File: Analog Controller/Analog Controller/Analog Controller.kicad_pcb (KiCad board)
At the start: 4 copper layers, 76.2 x 71.1 mm, 63 parts, among them J1 MINIFIT-2-VERT, J2 Conn_02x08_Counter_Clockwise, J3 Conn_02x08_Counter_Clockwise, J4 MINIFIT-2-VERT, J5 Conn_01x04, J6 MINIFIT-2-VERT, J7 Conn_02x09_Counter_Clockwise, J8 Conn_02x08_Counter_Clockwise, J9 284697-E, SW2 SW_Omron_B3FS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

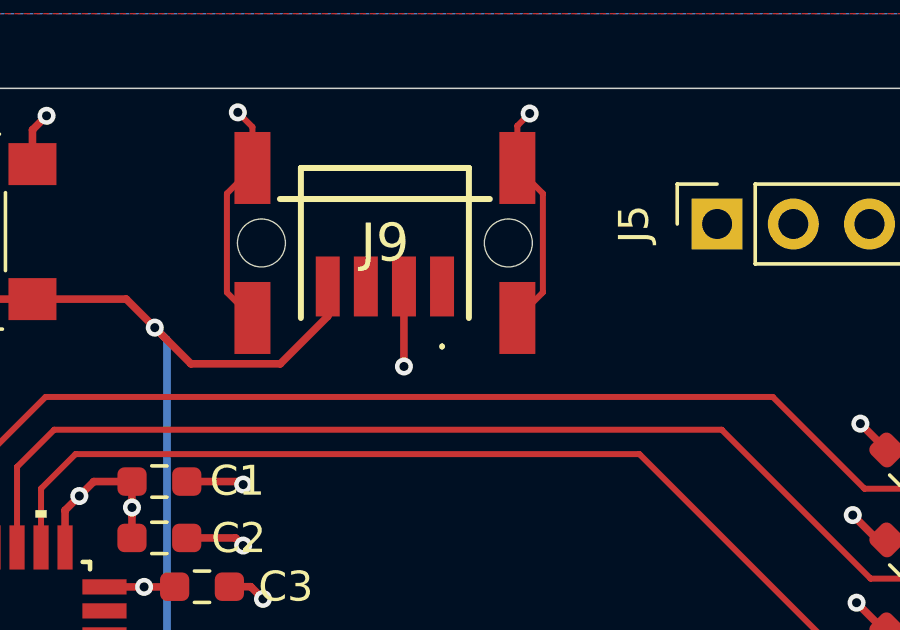
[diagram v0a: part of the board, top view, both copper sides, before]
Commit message: Reduced minimum clearance on digicorder
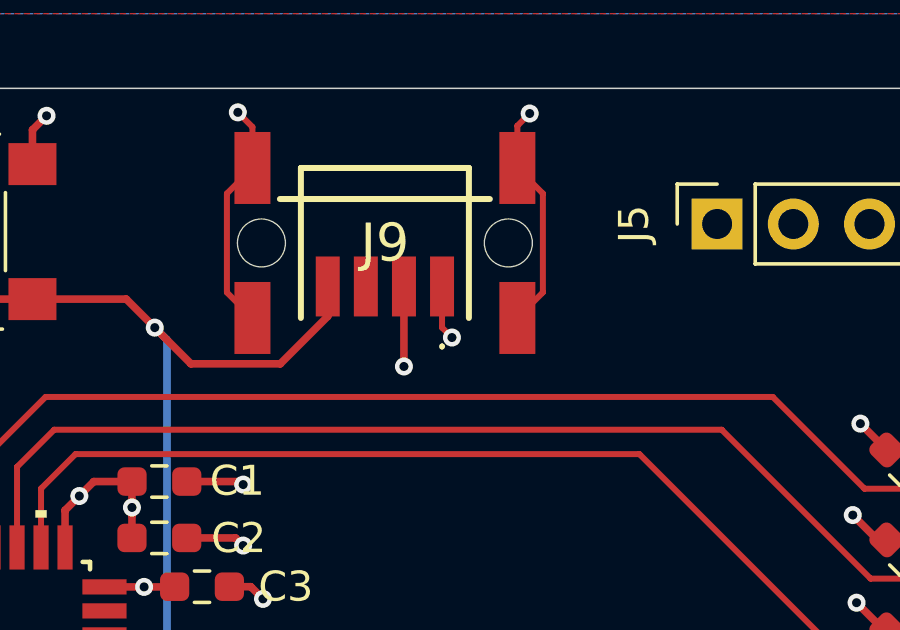
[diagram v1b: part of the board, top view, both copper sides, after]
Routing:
- net +3V3: track 28.5 -> 30.3 mm, vias 14 -> 15
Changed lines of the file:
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@@
+	)
+	(segment
+		(start 72.1614 33.3756)
+		(end 72.4916 33.7058)
+		(width 0.2)
+		(layer "F.Cu")
+		(net 2)
 	)
 	(segment
@@
 		(net 2)
 	)
+	(segment
+		(start 72.1614 32.004)
+		(end 72.1614 33.3756)
+		(width 0.2)
+		(layer "F.Cu")
+		(net 2)
+	)
 	(via
 		(at 63.3495 53.086)
@@
 		(size 0.6)
 		(drill 0.3)
+		(layers "F.Cu" "B.Cu")
+		(net 2)
+	)
+	(via
+		(at 72.4916 33.7058)
+		(size 0.6)
+		(drill 0.3)

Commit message: Added new stm32 microcontroller, redid pcb layout
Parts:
- removed C1, C20: 100n, Resistor_SMD:R_0603_1608Metric_Pad0.98x0.95mm_HandSolder
- removed C19, C3: 1u, Resistor_SMD:R_0603_1608Metric_Pad0.98x0.95mm_HandSolder
- removed C2: 10n, Resistor_SMD:R_0603_1608Metric_Pad0.98x0.95mm_HandSolder
- removed G***: LOGO, LOGO
- removed J5: Conn_01x04, Connector_PinSocket_2.54mm:PinSocket_1x04_P2.54mm_Vertical
- removed J9: 284697-E, 284697-E:284697E
- removed R10, R9: 4.7k, Resistor_SMD:R_0603_1608Metric_Pad0.98x0.95mm_HandSolder
- removed U10: TCA9535DBR, Package_SO:SSOP-24_5.3x8.2mm_P0.65mm
- removed U9: STM8L152K4T6, STM8L152K4T6:LQFP-32
- added C21: 10u, Resistor_SMD:R_0603_1608Metric_Pad0.98x0.95mm_HandSolder, F.Cu at (70.7, 45.6)
- added C22: 0.1u, Resistor_SMD:R_0603_1608Metric_Pad0.98x0.95mm_HandSolder, F.Cu at (54.5, 54.6)
- added C23: 0.1u, Resistor_SMD:R_0603_1608Metric_Pad0.98x0.95mm_HandSolder, F.Cu at (52.9, 42.8)
- added C24: 0.1u, Resistor_SMD:R_0603_1608Metric_Pad0.98x0.95mm_HandSolder, F.Cu at (54.9, 40.5)
- added C25: 0.1u, Resistor_SMD:R_0603_1608Metric_Pad0.98x0.95mm_HandSolder, F.Cu at (70.7, 43.8)
- added C26: 10n, Resistor_SMD:R_0603_1608Metric_Pad0.98x0.95mm_HandSolder, B.Cu at (63.4, 57.6)
- added C27: 1u, Resistor_SMD:R_0603_1608Metric_Pad0.98x0.95mm_HandSolder, B.Cu at (65.0, 57.6)
- added C28: 0.1u, Resistor_SMD:R_0603_1608Metric_Pad0.98x0.95mm_HandSolder, F.Cu at (51.6, 35.4)
- added C29: 0.1u, Resistor_SMD:R_0603_1608Metric_Pad0.98x0.95mm_HandSolder, B.Cu at (60.2, 57.6)
- added C30: 1u, Resistor_SMD:R_0603_1608Metric_Pad0.98x0.95mm_HandSolder, B.Cu at (61.8, 57.6)
- added J10: TC2050, Connector:Tag-Connect_TC2050-IDC-FP_2x05_P1.27mm_Vertical, F.Cu at (75.1, 34.7)
- added R14: 150, Resistor_SMD:R_0603_1608Metric_Pad0.98x0.95mm_HandSolder, F.Cu at (77.7, 28.6)
- added R15: 150, Resistor_SMD:R_0603_1608Metric_Pad0.98x0.95mm_HandSolder, F.Cu at (75.7, 28.6)
- added R16: 150, Resistor_SMD:R_0603_1608Metric_Pad0.98x0.95mm_HandSolder, F.Cu at (73.9, 28.6)
- added R17: 150, Resistor_SMD:R_0603_1608Metric_Pad0.98x0.95mm_HandSolder, F.Cu at (68.2, 33.4)
- added R18: 150, Resistor_SMD:R_0603_1608Metric_Pad0.98x0.95mm_HandSolder, F.Cu at (82.7, 35.3)
- added R19: 150, Resistor_SMD:R_0603_1608Metric_Pad0.98x0.95mm_HandSolder, F.Cu at (76.9, 40.8)
- added R20: 150, Resistor_SMD:R_0603_1608Metric_Pad0.98x0.95mm_HandSolder, F.Cu at (74.2, 40.7)
- added R21: 150, Resistor_SMD:R_0603_1608Metric_Pad0.98x0.95mm_HandSolder, F.Cu at (68.1, 35.3)
- added R22: 10k, Resistor_SMD:R_0603_1608Metric_Pad0.98x0.95mm_HandSolder, F.Cu at (56.3, 37.5)
- added R23: 150, Resistor_SMD:R_0603_1608Metric_Pad0.98x0.95mm_HandSolder, F.Cu at (58.0, 37.5)
- added SW4: SW_SPST, Button_Switch_SMD:SW_SPST_B3U-1000P, F.Cu at (61.4, 30.4)
- added U14: STM32G474RETx, Package_QFP:LQFP-64_10x10mm_P0.5mm, F.Cu at (61.0, 48.3)
- moved R3 15.0 mm to (87.2, 38.1)
- moved R6 9.10 mm to (86.9, 53.2)
- moved R7 9.10 mm to (86.9, 47.2)
- moved R8 9.10 mm to (86.9, 50.2)
- moved R2 8.98 mm to (87.2, 41.1)
- moved R13 3.89 mm to (84.6, 55.2)
- moved R11 3.84 mm to (84.6, 65.4)
- moved R12 3.83 mm to (84.6, 60.4)
- moved C15 3.48 mm to (89.9, 82.8)
- moved C14 3.48 mm to (90.2, 89.2)
- moved U8 3.48 mm to (89.8, 85.9)
- moved C12 3.41 mm to (75.8, 88.9)
- moved C13 3.41 mm to (75.8, 82.6)
- moved U7 3.41 mm to (75.6, 85.6)
- moved C11 3.33 mm to (69.3, 82.6)
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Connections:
- J2 pad 15: GND -> unconnected-(J2-Pin_15-Pad15)
- J2 pad 16: GND -> unconnected-(J2-Pin_16-Pad16)
- J2 pad 3: /CS_7 -> /CS_6
- J2 pad 5: /CS_6 -> /CS_7
- J2 pad 7: /SPI_CLK -> /MOSI
- J2 pad 8: /MOSI -> /SPI_CLK
- J3 pad 15: GND -> unconnected-(J3-Pin_15-Pad15)
- J3 pad 16: GND -> unconnected-(J3-Pin_16-Pad16)
- J3 pad 7: /SPI_CLK -> /MOSI
- J3 pad 8: /MOSI -> /SPI_CLK
- J7 pad 4: /POT_2 -> /Toggle_ON/OFF
- J7 pad 5: /POT_1 -> /ES_1
- J7 pad 6: /POT_0 -> /ES_0
- J7 pad 7: /Toggle_ON/OFF -> /POT_0
- J7 pad 8: /ES_1 -> /POT_1
- J7 pad 9: /ES_0 -> /POT_2
- J8 pad 15: GND -> unconnected-(J8-Pin_15-Pad15)
- J8 pad 16: GND -> unconnected-(J8-Pin_16-Pad16)
- J8 pad 7: /SPI_CLK -> /MOSI
- J8 pad 8: /MOSI -> /SPI_CLK
- SW2 pad 2: /STM32_MCU/RST -> /STM32_MCU/NRST
- U2 pad 6: /SPDT_1 -> /SPDT_0
- U3 pad 6: /SPDT_2 -> /SPDT_1
- U6 pad 6: /SPDT_3 -> /SPDT_1
- U7 pad 6: /SPDT_4 -> /SPDT_2
- U8 pad 6: /SPDT_5 -> /SPDT_2
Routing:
- net /SPDT_5: track 62.4 -> 0.00 mm, vias 2 -> 0
- net /SPDT_4: track 58.7 -> 0.00 mm, vias 2 -> 0
- net /SPDT_3: track 52.8 -> 0.00 mm, vias 2 -> 0
- net /STM32_MCU/UART_TX: track 46.6 -> 0.00 mm, vias 1 -> 0
- net /STM32_MCU/UART_RX: track 41.9 -> 0.00 mm, vias 1 -> 0
- net /STM32_MCU/NRST: track 0.00 -> 40.9 mm, vias 0 -> 2
- net /STM32_MCU/RST: track 36.6 -> 0.00 mm, vias 2 -> 0
- net /POT_0: track 34.3 -> 68.0 mm
- net /STM32_MCU/USART1_RX(MCU): track 0.00 -> 28.3 mm
- net /STM32_MCU/SWIM: track 26.7 -> 0.00 mm, vias 2 -> 0
- net /STM32_MCU/USART1_TX(MCU): track 0.00 -> 25.1 mm
- net /SPI_CLK: track 93.3 -> 72.5 mm
- net /STM32_MCU/I2C_SCL: track 20.4 -> 0.00 mm
- net /STM32_MCU/I2C_SDA: track 18.4 -> 0.00 mm, vias 2 -> 0
- net /MOSI: track 86.4 -> 70.9 mm
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
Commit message: Completed Power Board
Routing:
- net /CS_4: track 30.3 -> 31.0 mm
- net GND: vias 44 -> 43
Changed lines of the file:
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@@
 	)
 	(segment
+		(start 53.9762 51.51)
+		(end 53.7464 51.7398)
+		(width 0.2)
+		(layer "F.Cu")
+		(net 1)
+	)
+	(segment
 		(start 71.6261 45.5676)
 		(end 71.6261 43.8404)
@@
 	)
 	(segment
-		(start 55.285 51.51)
-		(end 54.34213 51.51)
-		(width 0.2)
-		(layer "F.Cu")
-		(net 1)
-	)
-	(segment
 		(start 48.9253 27.1912)
 		(end 48.5819 26.8478)
@@
 	)
 	(segment
-		(start 54.34213 51.51)
-		(end 53.865865 51.986265)
-		(width 0.2)
-		(layer "F.Cu")
-		(net 1)
-	)
-	(segment
 		(start 52.2014 85.0444)
 		(end 52.5218 84.724)
@@
 	)
 	(segment
+		(start 55.285 51.51)
+		(end 53.9762 51.51)
+		(width 0.2)
+		(layer "F.Cu")
+		(net 1)
+	)
+	(segment
 		(start 54.5338 56.5404)
 		(end 54.7624 56.769)
@@
 	)
 	(via
+		(at 53.7464 51.7398)
+		(size 0.6)
+		(drill 0.3)
+		(layers "F.Cu" "B.Cu")
+		(net 1)
+	)
+	(via
 		(at 52.5218 84.724)
 		(size 0.6)
@@
 	)
 	(via
-		(at 61.1758 58.4416)
-		(size 0.6)
-		(drill 0.3)
-		(layers "F.Cu" "B.Cu")
-		(net 1)
-	)
-	(via
 		(at 77.8256 89.2452)
 		(size 0.6)
@@
 	)
 	(via
-		(at 53.865865 51.986265)
-		(size 0.6)
-		(drill 0.3)
-		(layers "F.Cu" "B.Cu")
-		(net 1)
-	)
-	(via
 		(at 84.963 35.0012)
 		(size 0.6)
@@
 	)
 	(segment
-		(start 53.9936 51.01)
-		(end 53.1368 51.8668)
+		(start 52.705 51.7906)
+		(end 52.705 65.4812)
 		(width 0.2)
 		(layer "F.Cu")
@@
 	)
 	(segment
-		(start 53.1368 51.8668)
-		(end 53.1368 65.913)
+		(start 55.285 51.01)
+		(end 53.4856 51.01)
 		(width 0.2)
 		(layer "F.Cu")
@@
 	)
 	(segment
-		(start 56.1594 68.9356)
-		(end 56.1594 70.7644)
+		(start 53.4856 51.01)
+		(end 52.705 51.7906)
 		(width 0.2)
 		(layer "F.Cu")
@@
 	)
 	(segment
-		(start 55.285 51.01)
-		(end 53.9936 51.01)
+		(start 56.1594 68.9356)
+		(end 56.1594 70.7644)
 		(width 0.2)
 		(layer "F.Cu")
@@
 	)
 	(segment
-		(start 53.1368 65.913)
+		(start 52.705 65.4812)
 		(end 54.61 67.3862)
 		(width 0.2)
@@
 	)
 	(segment
-		(start 40.1828 60.8584)
-		(end 52.0312 49.01)
+		(start 40.1828 60.4266)
+		(end 51.5994 49.01)
 		(width 0.2)
 		(layer "F.Cu")
@@
 	)
 	(segment
-		(start 52.0312 49.01)
-		(end 55.285 49.01)
+		(start 42.545 73.66)
+		(end 40.1828 71.2978)
 		(width 0.2)
 		(layer "F.Cu")
@@
 	)
 	(segment
-		(start 42.545 73.66)
-		(end 40.1828 71.2978)
+		(start 51.5994 49.01)
+		(end 55.285 49.01)
 		(width 0.2)
 		(layer "F.Cu")
@@
 	(segment
 		(start 40.1828 71.2978)
-		(end 40.1828 60.8584)
+		(end 40.1828 60.4266)
 		(width 0.2)
 		(layer "F.Cu")
@@
 	)
 	(segment
-		(start 53.495 50.01)
-		(end 55.285 50.01)
+		(start 48.6664 72.6186)
+		(end 48.6664 54.0512)
 		(width 0.2)
 		(layer "F.Cu")
@@
 	)
 	(segment
-		(start 48.6664 72.6186)
-		(end 48.6664 54.8386)
+		(start 52.7076 50.01)
+		(end 55.285 50.01)
 		(width 0.2)
 		(layer "F.Cu")
@@
 	)
 	(segment
-		(start 45.085 76.2)
-		(end 48.6664 72.6186)
+		(start 48.6664 54.0512)
+		(end 52.7076 50.01)
 		(width 0.2)
 		(layer "F.Cu")
@@
 	)
 	(segment
-		(start 48.6664 54.8386)
-		(end 53.495 50.01)
+		(start 45.085 76.2)
+		(end 48.6664 72.6186)
 		(width 0.2)
 		(layer "F.Cu")
@@
 	)
 	(segment
-		(start 47.2948 54.9402)
-		(end 47.2948 71.4502)
+		(start 47.2948 71.4502)
+		(end 45.085 73.66)
 		(width 0.2)
 		(layer "F.Cu")
@@
 	)
 	(segment
-		(start 52.725001 49.509999)
-		(end 47.2948 54.9402)
+		(start 55.285 49.509999)
+		(end 52.166201 49.509999)
 		(width 0.2)
 		(layer "F.Cu")
@@
 	)
 	(segment
-		(start 55.285 49.509999)
-		(end 52.725001 49.509999)
+		(start 52.166201 49.509999)
+		(end 47.2948 54.3814)
 		(width 0.2)
 		(layer "F.Cu")
@@
 	)
 	(segment
-		(start 47.2948 71.4502)
-		(end 45.085 73.66)
+		(start 47.2948 54.3814)
+		(end 47.2948 71.4502)
 		(width 0.2)
 		(layer "F.Cu")
@@
 	)
 	(segment
-		(start 39.37 60.4266)
-		(end 51.2866 48.51)
+		(start 42.545 76.2)
+		(end 39.37 73.025)
 		(width 0.2)
 		(layer "F.Cu")
@@
 	)
 	(segment
-		(start 42.545 76.2)
-		(end 39.37 73.025)
+		(start 39.37 73.025)
+		(end 39.37 60.325)
 		(width 0.2)
 		(layer "F.Cu")
@@
 	)
 	(segment
-		(start 51.2866 48.51)
+		(start 51.185 48.51)
 		(end 55.285 48.51)
 		(width 0.2)
@@
 	)
 	(segment
-		(start 39.37 73.025)
-		(end 39.37 60.4266)
+		(start 39.37 60.325)
+		(end 51.185 48.51)
 		(width 0.2)
 		(layer "F.Cu")
@@
 	)
 	(segment
-		(start 55.285 50.51)
-		(end 53.9265 50.51)
+		(start 59.7916 76.8858)
+		(end 59.055 76.1492)
 		(width 0.2)
 		(layer "F.Cu")
@@
 	)
 	(segment
-		(start 59.7916 76.8858)
-		(end 59.055 76.1492)
+		(start 67.9704 85.298499)
+		(end 67.162899 85.298499)
 		(width 0.2)
 		(layer "F.Cu")
@@
 	)
 	(segment
-		(start 67.9704 85.298499)
-		(end 67.162899 85.298499)
+		(start 53.1474 50.51)
+		(end 52.2986 51.3588)
+		(width 0.2)
+		(layer "F.Cu")
+		(net 52)
+	)
+	(segment
+		(start 55.285 50.51)
+		(end 53.1474 50.51)
 		(width 0.2)
 		(layer "F.Cu")
@@
 	)
 	(segment
-		(start 53.9265 50.51)
-		(end 52.2986 52.1379)
+		(start 52.2986 51.3588)
+		(end 52.2986 69.3928)
 		(width 0.2)
 		(layer "F.Cu")
@@
 		(width 0.2)
 		(layer "F.Cu")
-		(net 52)
-	)
-	(segment
-		(start 52.2986 52.1379)
-		(end 52.2986 69.3928)
-		(width 0.2)
-		(layer "F.Cu")

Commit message: Incorporated changes from demo
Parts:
- added C1: 0.1u, Resistor_SMD:R_0603_1608Metric_Pad0.98x0.95mm_HandSolder, F.Cu at (93.5, 80.5)
- added R9: 240, Resistor_SMD:R_0603_1608Metric_Pad0.98x0.95mm_HandSolder, F.Cu at (93.5, 86.0)
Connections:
- U8 pad 1: /To_Dig_Board -> Net-(U8-COM)
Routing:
- net /To_Dig_Board: track 12.2 -> 9.26 mm
- net Net-(U8-COM): track 0.00 -> 2.49 mm
- net GND: track 62.0 -> 63.5 mm, vias 43 -> 44

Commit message: fixes for Marco's dr
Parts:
- added C2: 1u, Capacitor_SMD:C_0603_1608Metric, F.Cu at (33.3, 81.9)
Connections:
- U1 pad 1: /From_Preamp -> Net-(U1-COM)
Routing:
- net /From_Preamp: track 9.14 -> 5.28 mm
- net Net-(U1-COM): track 0.00 -> 3.22 mm
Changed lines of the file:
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@@
 	(net 104 "unconnected-(J8-Pin_16-Pad16)")
 	(net 105 "Net-(U8-COM)")
+	(net 106 "Net-(U1-COM)")
 	(footprint "MountingHole:MountingHole_3.2mm_M3"
 		(layer "F.Cu")
@@
 			(size 3.2 3.2)
 			(drill 3.2)
-			(layers "*.Cu" "*.Mask")
+			(layers "F&B.Cu" "*.Mask")
+			(clearance 2)
 		)
 		(embedded_fonts no)
@@
 			(size 1.3208 0.4318)
 			(layers "F.Cu" "F.Mask" "F.Paste")
-			(net 5 "/From_Preamp")
+			(net 106 "Net-(U1-COM)")
 			(pinfunction "COM")
 			(pintype "bidirectional")
@@
 		(embedded_fonts no)
 	)
+	(footprint "Capacitor_SMD:C_0603_1608Metric"
+		(layer "F.Cu")
+		(at 33.325706 81.900539 -90)
+		(descr "Capacitor SMD 0603 (1608 Metric), square (rectangular) end terminal, IPC-7351 nominal, (Body size source: IPC-SM-782 page 76, https://www.pcb-3d.com/wordpress/wp-content/uploads/ipc-sm-782a_amendment_1_and_2.pdf), generated with kicad-footprint-generator")
+		(tags "capacitor")
+		(property "Reference" "C2"
+			(at -2.494128 -0.205074 90)
+			(layer "F.SilkS")
+			(effects
+				(font
+					(size 1 1)
+					(thickness 0.15)
+				)
+			)
+		)
+		(property "Value" "1u"
+			(at 0 1.43 90)
+			(layer "F.Fab")
+			(effects
+				(font
+					(size 1 1)
+					(thickness 0.15)
+				)
+			)
+		)
+		(property "Datasheet" "~"
+			(at 0 0 90)
+			(layer "F.Fab")
+			(hide yes)
+			(effects
+				(font
+					(size 1.27 1.27)
+					(thickness 0.15)
+				)
+			)
+		)
+		(property "Description" "Unpolarized capacitor"
+			(at 0 0 90)
+			(layer "F.Fab")
+			(hide yes)
+			(effects
+				(font
+					(size 1.27 1.27)
+					(thickness 0.15)
+				)
+			)
+		)
+		(property ki_fp_filters "C_*")
+		(sheetname "/")
+		(sheetfile "Analog Controller.kicad_sch")
+		(attr smd)
+		(fp_line
+			(start -0.14058 0.51)
+			(end 0.14058 0.51)
+			(stroke
+				(width 0.12)
+				(type solid)
+			)
+			(layer "F.SilkS")
+		)
+		(fp_line
+			(start -0.14058 -0.51)
+			(end 0.14058 -0.51)
+			(stroke
+				(width 0.12)
+				(type solid)
+			)
+			(layer "F.SilkS")
+		)
+		(fp_line
+			(start -1.48 0.73)
+			(end -1.48 -0.73)
+			(stroke
+				(width 0.05)
+				(type solid)
+			)
+			(layer "F.CrtYd")
+		)
+		(fp_line
+			(start 1.48 0.73)
+			(end -1.48 0.73)
+			(stroke
+				(width 0.05)
+				(type solid)
+			)
+			(layer "F.CrtYd")
+		)
+		(fp_line
+			(start -1.48 -0.73)
+			(end 1.48 -0.73)
+			(stroke
+				(width 0.05)
+				(type solid)
+			)
+			(layer "F.CrtYd")
+		)
+		(fp_line
+			(start 1.48 -0.73)
+			(end 1.48 0.73)
+			(stroke
+				(width 0.05)
+				(type solid)
+			)
+			(layer "F.CrtYd")
+		)
+		(fp_line
+			(start -0.8 0.4)
+			(end -0.8 -0.4)
+			(stroke
+				(width 0.1)
+				(type solid)
+			)
+			(layer "F.Fab")
+		)
+		(fp_line
+			(start 0.8 0.4)
+			(end -0.8 0.4)
+			(stroke
+				(width 0.1)
+				(type solid)
+			)
+			(layer "F.Fab")
+		)
+		(fp_line
+			(start -0.8 -0.4)
+			(end 0.8 -0.4)
+			(stroke
+				(width 0.1)
+				(type solid)
+			)
+			(layer "F.Fab")
+		)
+		(fp_line
+			(start 0.8 -0.4)
+			(end 0.8 0.4)
+			(stroke
+				(width 0.1)
+				(type solid)
+			)
+			(layer "F.Fab")
+		)
+		(fp_text user "${REFERENCE}"
+			(at 0 0 90)
+			(layer "F.Fab")
+			(effects
+				(font
+					(size 0.4 0.4)
+					(thickness 0.06)
+				)
+			)
+		)
+		(pad "1" smd roundrect
+			(at -0.775 0 270)
+			(size 0.9 0.95)
+			(layers "F.Cu" "F.Mask" "F.Paste")
+			(roundrect_rratio 0.25)
+			(net 5 "/From_Preamp")
+			(pintype "passive")
+		)
+		(pad "2" smd roundrect
+			(at 0.775 0 270)
+			(size 0.9 0.95)
+			(layers "F.Cu" "F.Mask" "F.Paste")
+			(roundrect_rratio 0.25)
+			(net 106 "Net-(U1-COM)")
+			(pintype "passive")
+		)
+		(embedded_fonts no)
+		(model "${KICAD9_3DMODEL_DIR}/Capacitor_SMD.3dshapes/C_0603_1608Metric.step"
+			(offset
+				(xyz 0 0 0)
+			)
+			(scale
+				(xyz 1 1 1)
+			)
+			(rotate
+				(xyz 0 0 0)
+			)
+		)
+	)
 	(footprint "Connector_Molex:Molex_Micro-Fit_3.0_43045-1812_2x09_P3.00mm_Vertical"
 		(layer "F.Cu")
@@
 			(size 3.2 3.2)
 			(drill 3.2)
-			(layers "*.Cu" "*.Mask")
+			(layers "F&B.Cu" "*.Mask")
+			(clearance 2)
 		)
 		(embedded_fonts no)
@@
 			(size 3.2 3.2)
 			(drill 3.2)
-			(layers "*.Cu" "*.Mask")
+			(layers "F&B.Cu" "*.Mask")
+			(clearance 2)
 		)
 		(embedded_fonts no)
@@
 			(size 3.2 3.2)
 			(drill 3.2)
-			(layers "*.Cu" "*.Mask")
+			(layers "F&B.Cu" "*.Mask")
+			(clearance 2)
 		)
 		(embedded_fonts no)
@@
 	)
 	(segment
-		(start 29.21 78.32)
-		(end 35.030402 84.140402)
+		(start 32.015539 81.125539)
+		(end 29.21 78.32)
 		(width 0.2)
 		(layer "F.Cu")
@@
 	)
 	(segment
-		(start 35.030402 84.140402)
-		(end 35.941 84.140402)
+		(start 33.325706 81.125539)
+		(end 32.015539 81.125539)
 		(width 0.2)
 		(layer "F.Cu")
@@
 		(net 105)
 	)
+	(segment
+		(start 34.790569 84.140402)
+		(end 35.941 84.140402)
+		(width 0.2)
+		(layer "F.Cu")
+		(net 106)
+	)
+	(segment
+		(start 33.325706 82.675539)
+		(end 34.790569 84.140402)
+		(width 0.2)
+		(layer "F.Cu")
+		(net 106)
+	)
 	(zone
